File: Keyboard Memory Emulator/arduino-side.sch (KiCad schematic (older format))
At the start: 15 parts, among them J4 Conn_01x03, SW1 PTS636 SL43 LFS, U10 SN74HC244APWR, U11 SN74HC244APWR, U12 74LV245APWJ, U8 ATmega32-16AU, U9 MC74VHC1G04DBVT1G, Y1 32.768kHz

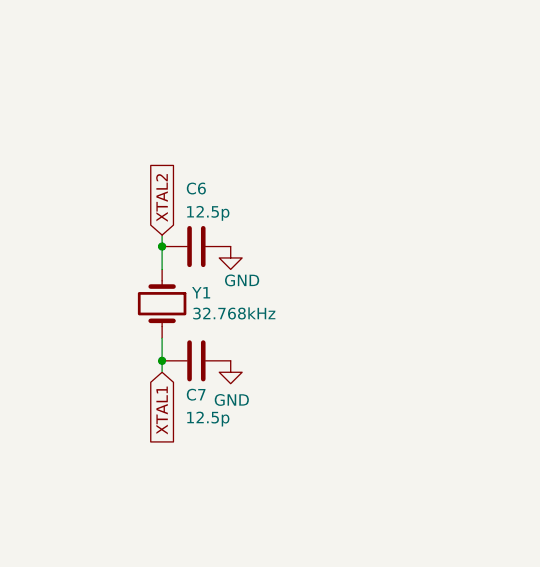
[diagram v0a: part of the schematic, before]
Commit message: Ran the autorouter and updated the PCB
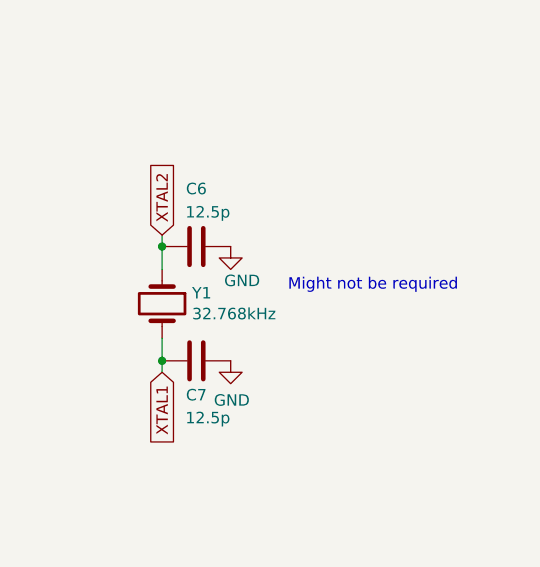
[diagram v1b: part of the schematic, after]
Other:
- note added: "Might not be required\n"
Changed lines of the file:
@@
 	7650 4300 7650 4250
 Connection ~ 7650 4250
+Text Notes 8200 3950 0    50   ~ 0
+Might not be required\n
 $EndSCHEMATC

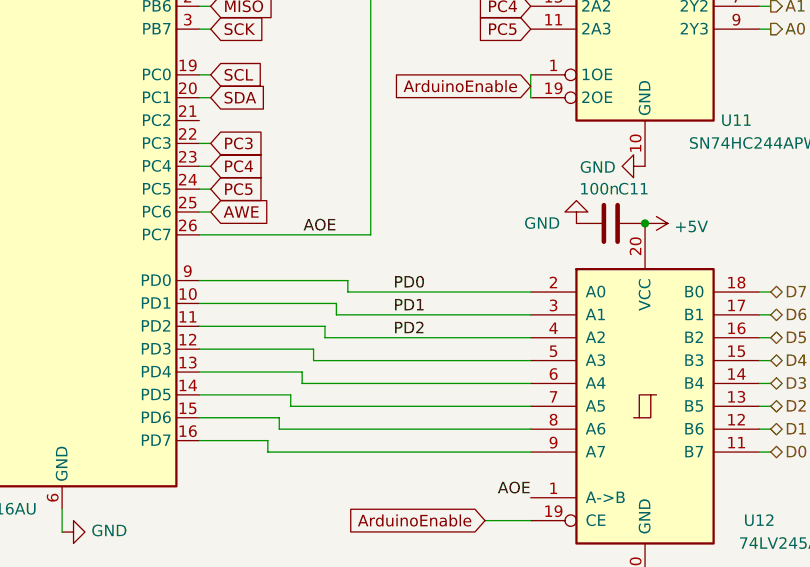
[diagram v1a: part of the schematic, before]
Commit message: Added a gitignore, hopefully it will work as I hope. I also fixed the traces that were not showing up due to improper nets.
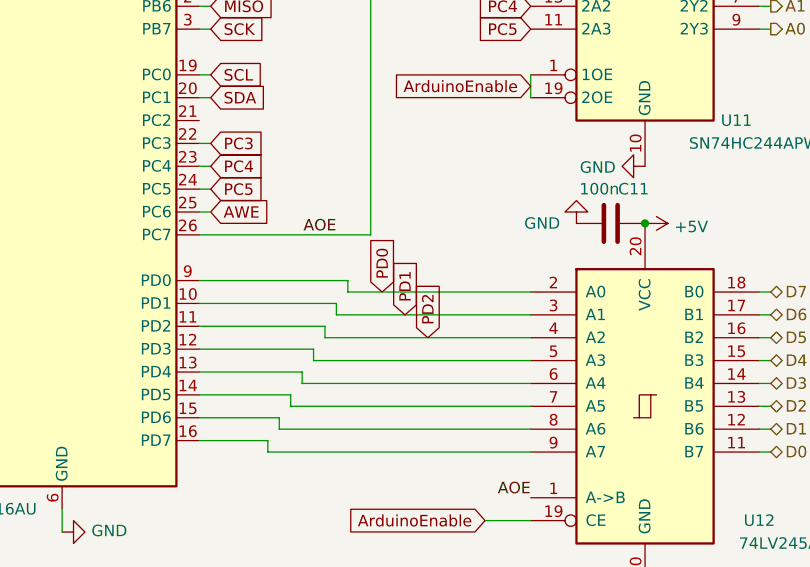
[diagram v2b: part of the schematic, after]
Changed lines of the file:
@@
 Title "Keyboard Memory Emulator"
 Date "2020-11-29"
-Rev "P-0"
+Rev "P-1"
 Comp "Mason Gulu, Lucas Christy"
 Comment1 ""
@@
 Wire Wire Line
 	3650 4400 3600 4400
-Text Label 4450 5050 0    50   ~ 0
-PD0
-Text Label 4450 5150 0    50   ~ 0
-PD1
-Text Label 4450 5250 0    50   ~ 0
-PD2
 Text GLabel 3650 3900 2    50   Input ~ 0
 SCK
@@
 Text Notes 8200 3950 0    50   ~ 0
 Might not be required\n
+Text GLabel 4400 5050 1    50   Input ~ 0
+PD0
+Text GLabel 4500 5150 1    50   Input ~ 0
+PD1
+Text GLabel 4600 5250 1    50   Input ~ 0
+PD2
 $EndSCHEMATC
